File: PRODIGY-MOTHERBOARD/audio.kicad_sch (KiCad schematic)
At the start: 7 parts, among them J15 AudioJack3, U7 LM386, U8 Si4460, U9 LM386

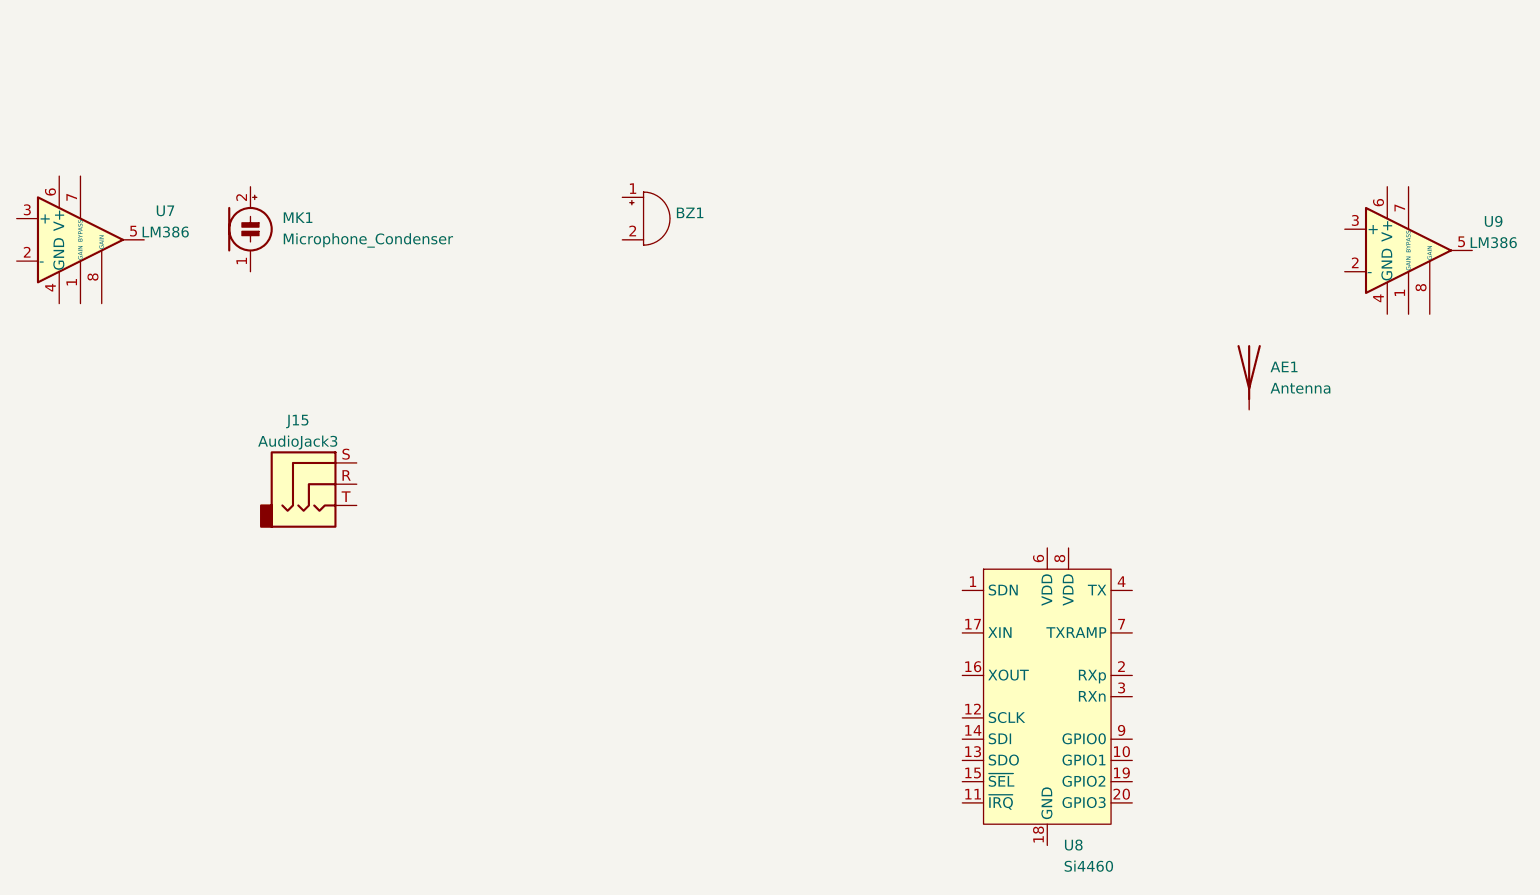
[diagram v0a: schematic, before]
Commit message: project restructure done. Hierarchical sheet done. Outputs/breakouts sheet done
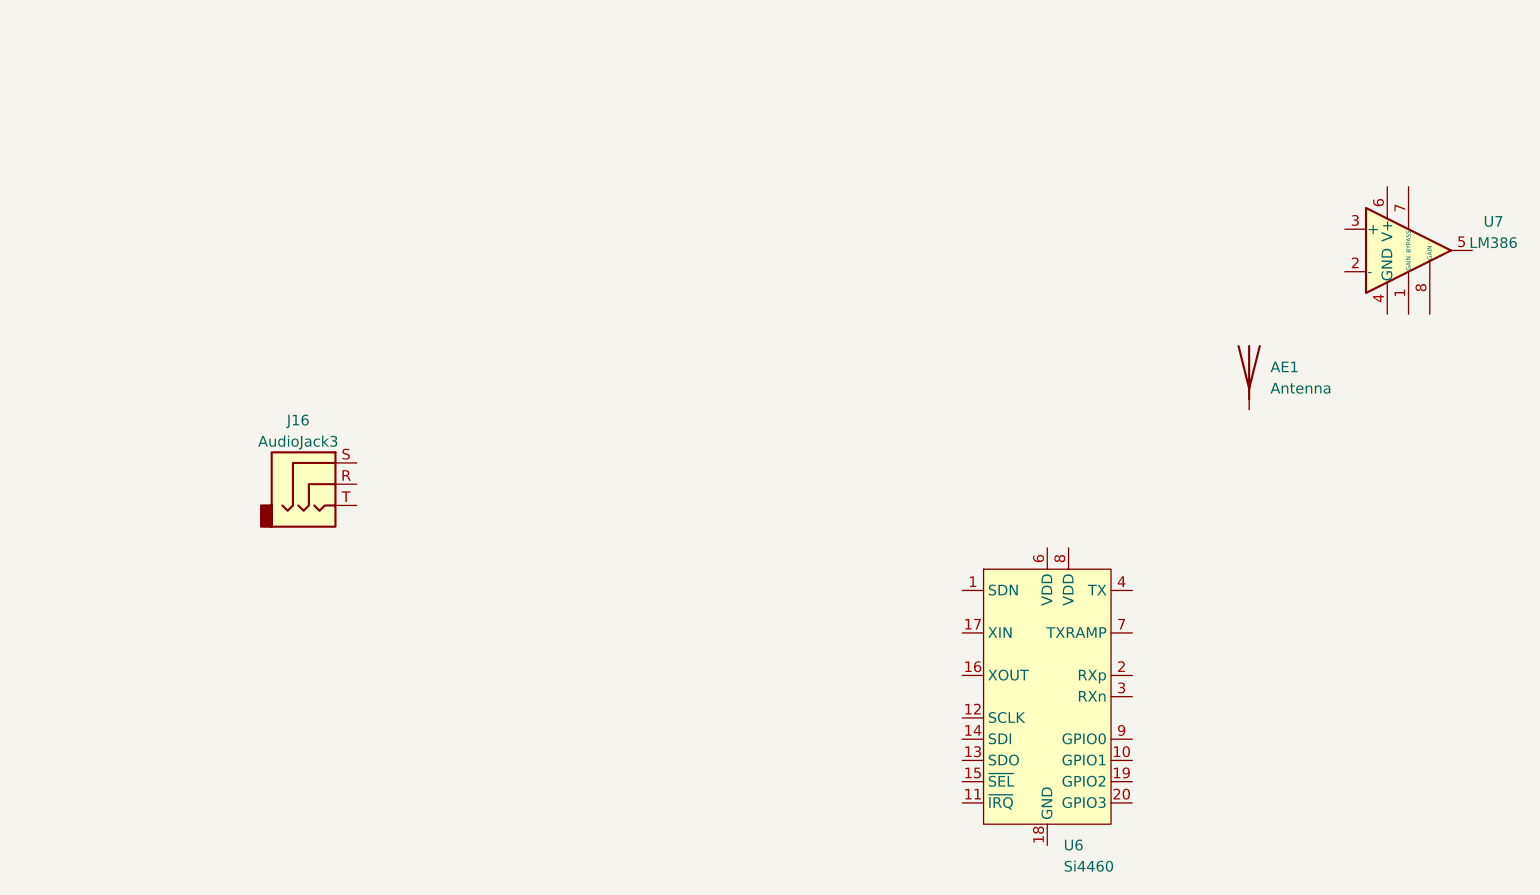
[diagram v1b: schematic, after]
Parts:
- removed BZ1: Buzzer, Buzzer_Beeper:MagneticBuzzer_ProSignal_ABI-010-RC, symbol Device:Buzzer
- removed MK1: Microphone_Condenser, Buzzer_Beeper:MagneticBuzzer_Kingstate_KCG0601, symbol Device:Microphone_Condenser
- removed U7: LM386, Package_SO:SOP-8_3.9x4.9mm_P1.27mm, symbol Amplifier_Audio:LM386
- renumbered J15 to J16, U8 to U6, U9 to U7

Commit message: Finished neopixel and button's schematic.
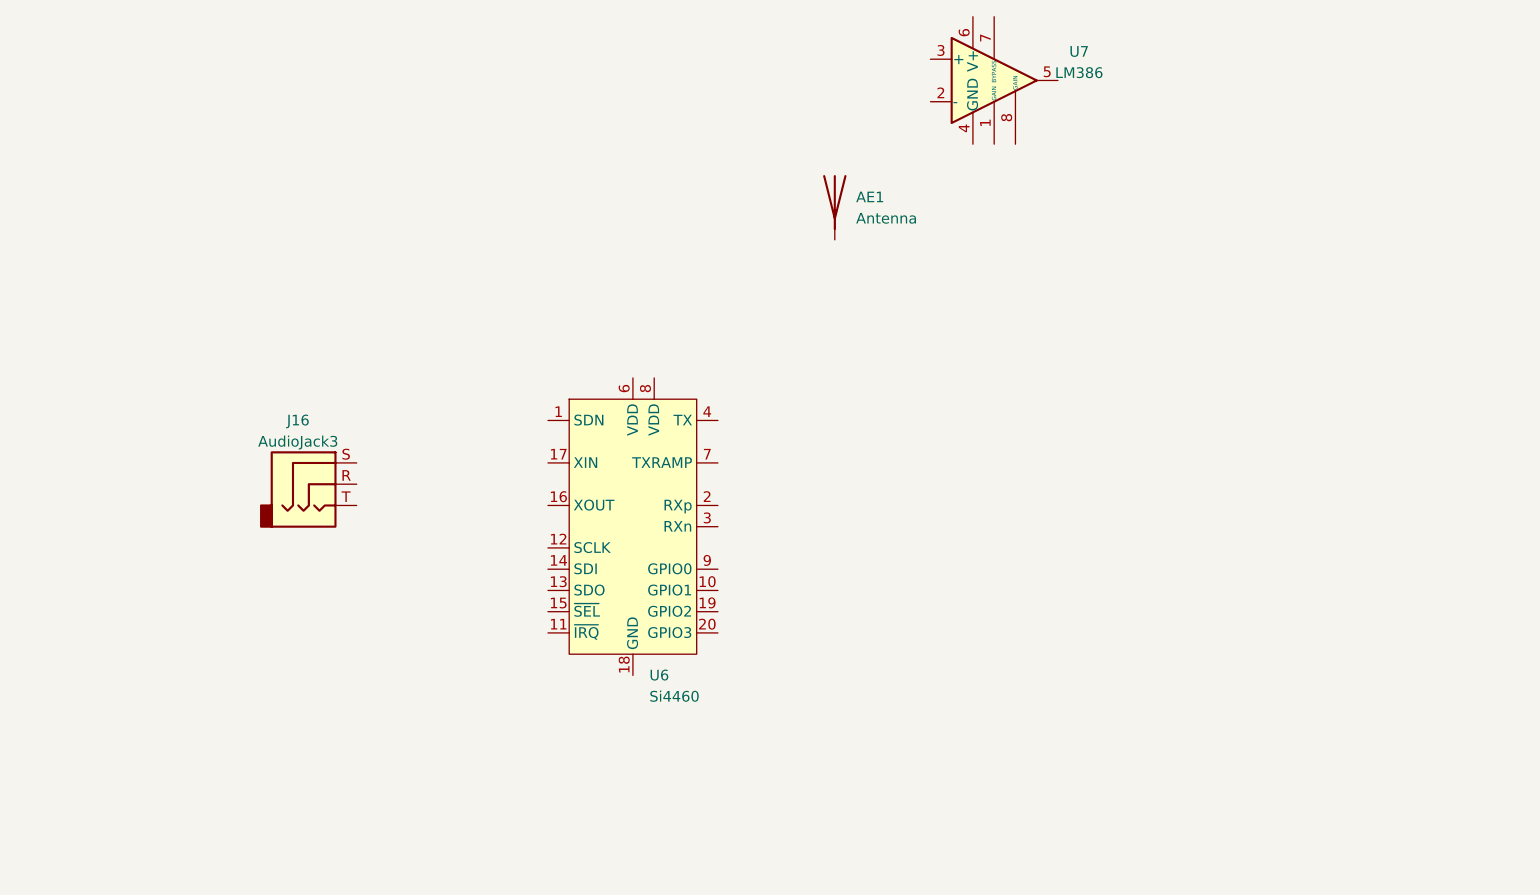
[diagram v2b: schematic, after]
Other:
- moved on the sheet: AE1, U6, U7
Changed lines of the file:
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@@
 	(symbol
 		(lib_id "Device:Antenna")
-		(at 222.25 78.74 0)
+		(at 172.72 58.42 0)
 		(unit 1)
 		(exclude_from_sim no)
@@
 		(fields_autoplaced yes)
 		(property "Reference" "AE1"
-			(at 224.79 78.74 0)
+			(at 175.26 58.42 0)
 			(effects
 				(font
@@
 		)
 		(property "Value" "Antenna"
-			(at 224.79 81.28 0)
+			(at 175.26 60.96 0)
 			(effects
 				(font
@@
 		)
 		(property "Footprint" "Connector_PinSocket_2.54mm:PinSocket_1x01_P2.54mm_Vertical"
-			(at 222.25 78.74 0)
+			(at 172.72 58.42 0)
 			(effects
 				(font
@@
 		)
 		(property "Datasheet" "~"
-			(at 222.25 78.74 0)
-			(effects
-				(font
-					(size 1.27 1.27)
-				)
-				(hide yes)
-			)
-		)
-		(property "Description" ""
-			(at 222.25 78.74 0)
+			(at 172.72 58.42 0)
+			(effects
+				(font
+					(size 1.27 1.27)
+				)
+				(hide yes)
+			)
+		)
+		(property "Description" ""
+			(at 172.72 58.42 0)
 			(effects
 				(font
@@
 	(symbol
 		(lib_id "RF:Si4460")
-		(at 198.12 118.11 0)
+		(at 148.59 97.79 0)
 		(unit 1)
 		(exclude_from_sim no)
@@
 		(fields_autoplaced yes)
 		(property "Reference" "U6"
-			(at 200.0759 135.89 0)
+			(at 150.5459 115.57 0)
 			(effects
 				(font
@@
 		)
 		(property "Value" "Si4460"
-			(at 200.0759 138.43 0)
+			(at 150.5459 118.11 0)
 			(effects
 				(font
@@
 		)
 		(property "Footprint" "Package_DFN_QFN:QFN-20-1EP_4x4mm_P0.5mm_EP2.5x2.5mm"
-			(at 198.12 87.63 0)
+			(at 148.59 67.31 0)
 			(effects
 				(font
@@
 		)
 		(property "Datasheet" "https://www.silabs.com/documents/public/data-sheets/Si4464-63-61-60.pdf"
-			(at 190.5 120.65 0)
-			(effects
-				(font
-					(size 1.27 1.27)
-				)
-				(hide yes)
-			)
-		)
-		(property "Description" ""
-			(at 198.12 118.11 0)
+			(at 140.97 100.33 0)
+			(effects
+				(font
+					(size 1.27 1.27)
+				)
+				(hide yes)
+			)
+		)
+		(property "Description" ""
+			(at 148.59 97.79 0)
 			(effects
 				(font
@@
 	(symbol
 		(lib_id "Amplifier_Audio:LM386")
-		(at 241.3 64.77 0)
+		(at 191.77 44.45 0)
 		(unit 1)
 		(exclude_from_sim no)
@@
 		(fields_autoplaced yes)
 		(property "Reference" "U7"
-			(at 251.46 61.3411 0)
+			(at 201.93 41.0211 0)
 			(effects
 				(font
@@
 		)
 		(property "Value" "LM386"
-			(at 251.46 63.8811 0)
+			(at 201.93 43.5611 0)
 			(effects
 				(font
@@
 		)
 		(property "Footprint" "Package_SO:SOP-8_3.9x4.9mm_P1.27mm"
-			(at 243.84 62.23 0)
+			(at 194.31 41.91 0)
 			(effects
 				(font
@@
 		)
 		(property "Datasheet" "http://www.ti.com/lit/ds/symlink/lm386.pdf"
-			(at 246.38 59.69 0)
-			(effects
-				(font
-					(size 1.27 1.27)
-				)
-				(hide yes)
-			)
-		)
-		(property "Description" ""
-			(at 241.3 64.77 0)
-			(effects
-				(font
+			(at 196.85 39.37 0)
+			(effects
+				(font
+					(size 1.27 1.27)
+				)
+				(hide yes)
+			)
+		)
+		(property "Description" ""
+			(at 191.77 44.45 0)
+			(effects
+				(font

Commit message: CAN schematic done
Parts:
- renumbered J16 to J24, U6 to U8, U7 to U9
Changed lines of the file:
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@@
 		(dnp no)
 		(fields_autoplaced yes)
-		(property "Reference" "J16"
+		(property "Reference" "J24"
 			(at 108.585 85.09 0)
 			(effects
@@
 			(project "PRODIGY-MOTHERBOARD"
 				(path "/f1c25860-8989-4190-bd24-2491d23ca7d9/e2913798-f444-47a6-8b64-53020d7d816b/beae7986-1156-4b71-ad5e-6c6ef7c2c7f1"
-					(reference "J16")
+					(reference "J24")
 					(unit 1)
 				)
@@
 		(dnp no)
 		(fields_autoplaced yes)
-		(property "Reference" "U6"
+		(property "Reference" "U8"
 			(at 150.5459 115.57 0)
 			(effects
@@
 			(project "PRODIGY-MOTHERBOARD"
 				(path "/f1c25860-8989-4190-bd24-2491d23ca7d9/e2913798-f444-47a6-8b64-53020d7d816b/beae7986-1156-4b71-ad5e-6c6ef7c2c7f1"
-					(reference "U6")
+					(reference "U8")
 					(unit 1)
 				)
@@
 		(dnp no)
 		(fields_autoplaced yes)
-		(property "Reference" "U7"
+		(property "Reference" "U9"
 			(at 201.93 41.0211 0)
 			(effects
@@
 			(project "PRODIGY-MOTHERBOARD"
 				(path "/f1c25860-8989-4190-bd24-2491d23ca7d9/e2913798-f444-47a6-8b64-53020d7d816b/beae7986-1156-4b71-ad5e-6c6ef7c2c7f1"
-					(reference "U7")
+					(reference "U9")
 					(unit 1)
 				)

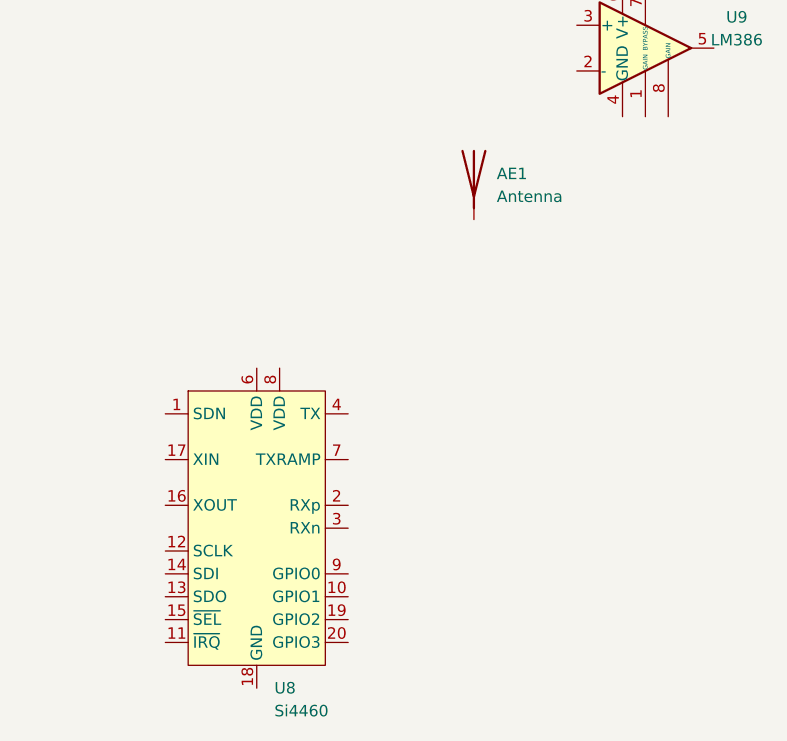
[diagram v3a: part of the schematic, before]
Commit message: SPI NFC schematic done.
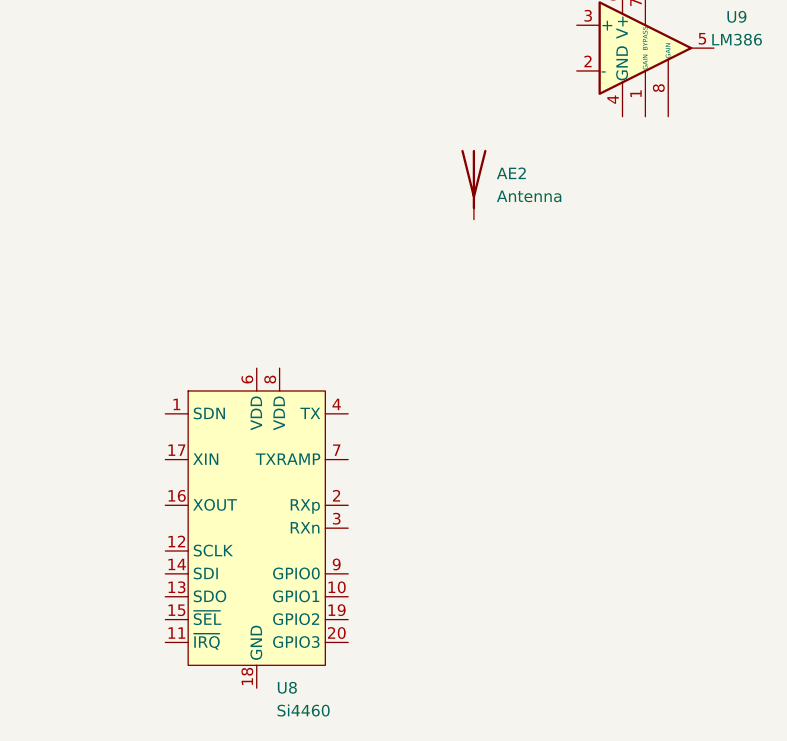
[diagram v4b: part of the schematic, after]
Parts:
- renumbered AE1 to AE2
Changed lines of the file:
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@@
 		(dnp no)
 		(fields_autoplaced yes)
-		(property "Reference" "AE1"
+		(property "Reference" "AE2"
 			(at 175.26 58.42 0)
 			(effects
@@
 			(project "PRODIGY-MOTHERBOARD"
 				(path "/f1c25860-8989-4190-bd24-2491d23ca7d9/e2913798-f444-47a6-8b64-53020d7d816b/beae7986-1156-4b71-ad5e-6c6ef7c2c7f1"
-					(reference "AE1")
+					(reference "AE2")
 					(unit 1)
 				)
@@
 		(fields_autoplaced yes)
 		(property "Reference" "U8"
-			(at 150.5459 115.57 0)
+			(at 150.7841 115.57 0)
 			(effects
 				(font
@@
 		)
 		(property "Value" "Si4460"
-			(at 150.5459 118.11 0)
+			(at 150.7841 118.11 0)
 			(effects
 				(font

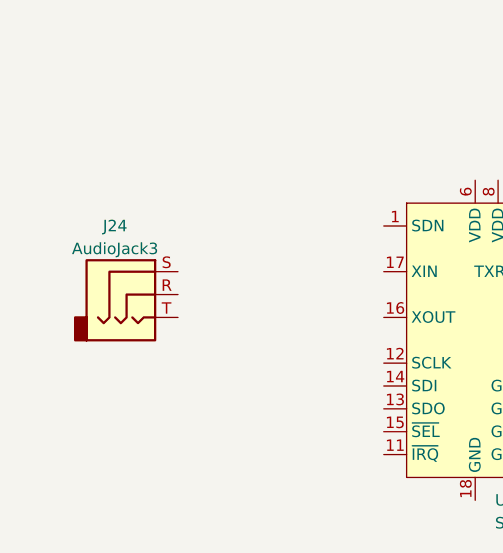
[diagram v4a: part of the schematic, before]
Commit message: Analog schematic finished, except the joystick part.
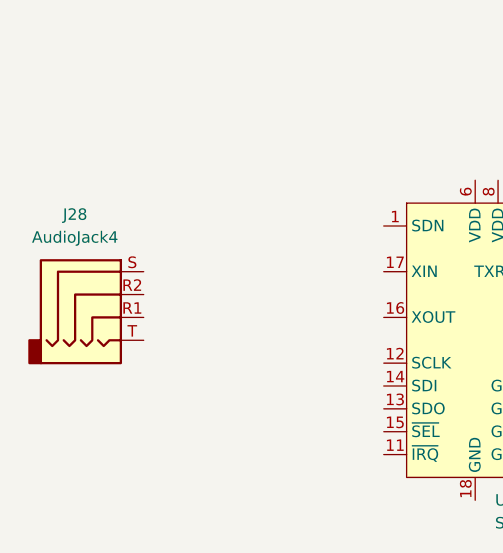
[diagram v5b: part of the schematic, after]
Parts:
- removed J24: AudioJack3, Connector_Audio:Jack_3.5mm_Lumberg_1503_07_Horizontal, symbol Connector_Audio:AudioJack3
- added J28: AudioJack4, Connector_Audio:Jack_3.5mm_KoreanHropartsElec_PJ-320D-4A_Horizontal, symbol Connector_Audio:AudioJack4
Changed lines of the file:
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@@
-	)
-	(symbol
-		(lib_id "Connector_Audio:AudioJack3")
-		(at 110.49 92.71 0)
-		(unit 1)
-		(exclude_from_sim no)
-		(in_bom yes)
-		(on_board yes)
-		(dnp no)
-		(fields_autoplaced yes)
-		(property "Reference" "J24"
-			(at 108.585 85.09 0)
-			(effects
-				(font
-					(size 1.27 1.27)
-				)
-			)
-		)
-		(property "Value" "AudioJack3"
-			(at 108.585 87.63 0)
-			(effects
-				(font
-					(size 1.27 1.27)
-				)
-			)
-		)
-		(property "Footprint" "Connector_Audio:Jack_3.5mm_Lumberg_1503_07_Horizontal"
-			(at 110.49 92.71 0)
-			(effects
-				(font
-					(size 1.27 1.27)
-				)
-				(hide yes)
-			)
-		)
-		(property "Datasheet" "~"
-			(at 110.49 92.71 0)
-			(effects
-				(font
-					(size 1.27 1.27)
-				)
-				(hide yes)
-			)
-		)
-		(property "Description" ""
-			(at 110.49 92.71 0)
-			(effects
-				(font
-					(size 1.27 1.27)
-				)
-				(hide yes)
-			)
-		)
-		(pin "R"
-		)
-		(pin "S"
-		)
-		(pin "T"
-		)
-		(instances
-			(project "PRODIGY-MOTHERBOARD"
-				(path "/f1c25860-8989-4190-bd24-2491d23ca7d9/e2913798-f444-47a6-8b64-53020d7d816b/beae7986-1156-4b71-ad5e-6c6ef7c2c7f1"
-					(reference "J24")
-					(unit 1)
-				)
-			)
-		)
 	)
 	(symbol
@@
 					(unit 1)
 				)
+			)
+		)
+	)
+	(symbol
+		(lib_id "Connector_Audio:AudioJack4")
+		(at 106.68 92.71 0)
+		(unit 1)
+		(exclude_from_sim no)
+		(in_bom yes)
+		(on_board yes)
+		(dnp no)
+		(fields_autoplaced yes)
+		(property "Reference" "J28"
+			(at 104.14 83.82 0)
+			(effects
+				(font
+					(size 1.27 1.27)
+				)
+			)
+		)
+		(property "Value" "AudioJack4"
+			(at 104.14 86.36 0)
+			(effects
+				(font
+					(size 1.27 1.27)
+				)
+			)
+		)
+		(property "Footprint" "Connector_Audio:Jack_3.5mm_KoreanHropartsElec_PJ-320D-4A_Horizontal"
+			(at 106.68 92.71 0)
+			(effects
+				(font
+					(size 1.27 1.27)
+				)
+				(hide yes)
+			)
+		)
+		(property "Datasheet" "~"
+			(at 106.68 92.71 0)
+			(effects
+				(font
+					(size 1.27 1.27)
+				)
+				(hide yes)
+			)
+		)
+		(property "Description" "Audio Jack, 4 Poles (TRRS)"
+			(at 106.68 92.71 0)
+			(effects
+				(font
+					(size 1.27 1.27)
+				)
+				(hide yes)
+			)
+		)
+		(pin "R1"
+		)
+		(pin "T"
+		)
+		(pin "S"
+		)
+		(pin "R2"
+		)
+		(instances
+			(project "PRODIGY-MOTHERBOARD"
+				(path "/f1c25860-8989-4190-bd24-2491d23ca7d9/e2913798-f444-47a6-8b64-53020d7d816b/beae7986-1156-4b71-ad5e-6c6ef7c2c7f1"
+					(reference "J28")
+					(unit 1)
+				)
